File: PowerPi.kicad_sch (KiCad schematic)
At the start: 34 parts, among them J1 2444, J3 Conn_01x02, J6 Raspberry_Pi_2_3, J8 2444, Q1 30V 4A 44mΩ, Q2 50nA 150V 200mW 200mA, Q3 30V 4A 44mΩ, U1 XL4015

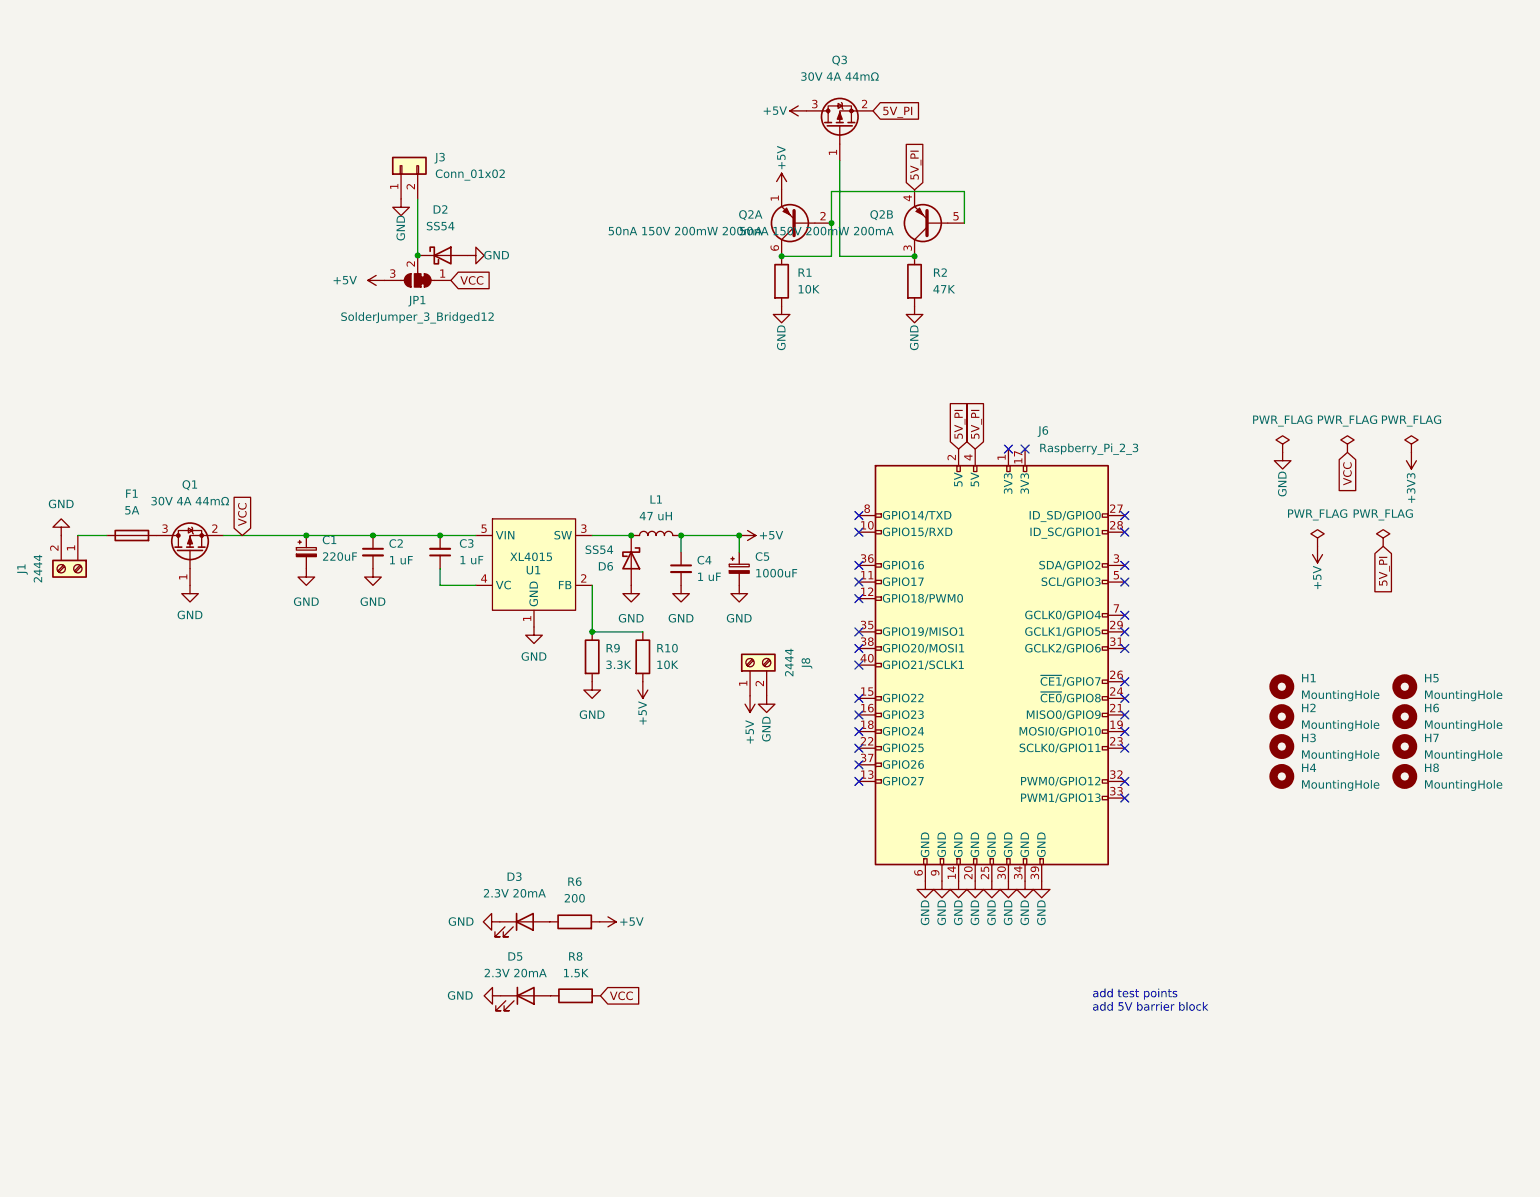
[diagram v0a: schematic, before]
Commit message: Production Changes
Added LDO Naming to R.silk
Fan JST XH pin +5 and GND swapped to match standard fans
5V pwr LED resistor was 200R now 1KR
24v pwr LED was 1.5k now 10k
Changed sch symbol for XH to not have screws
Added boxes to schematic layout
Added title box entries to schematic
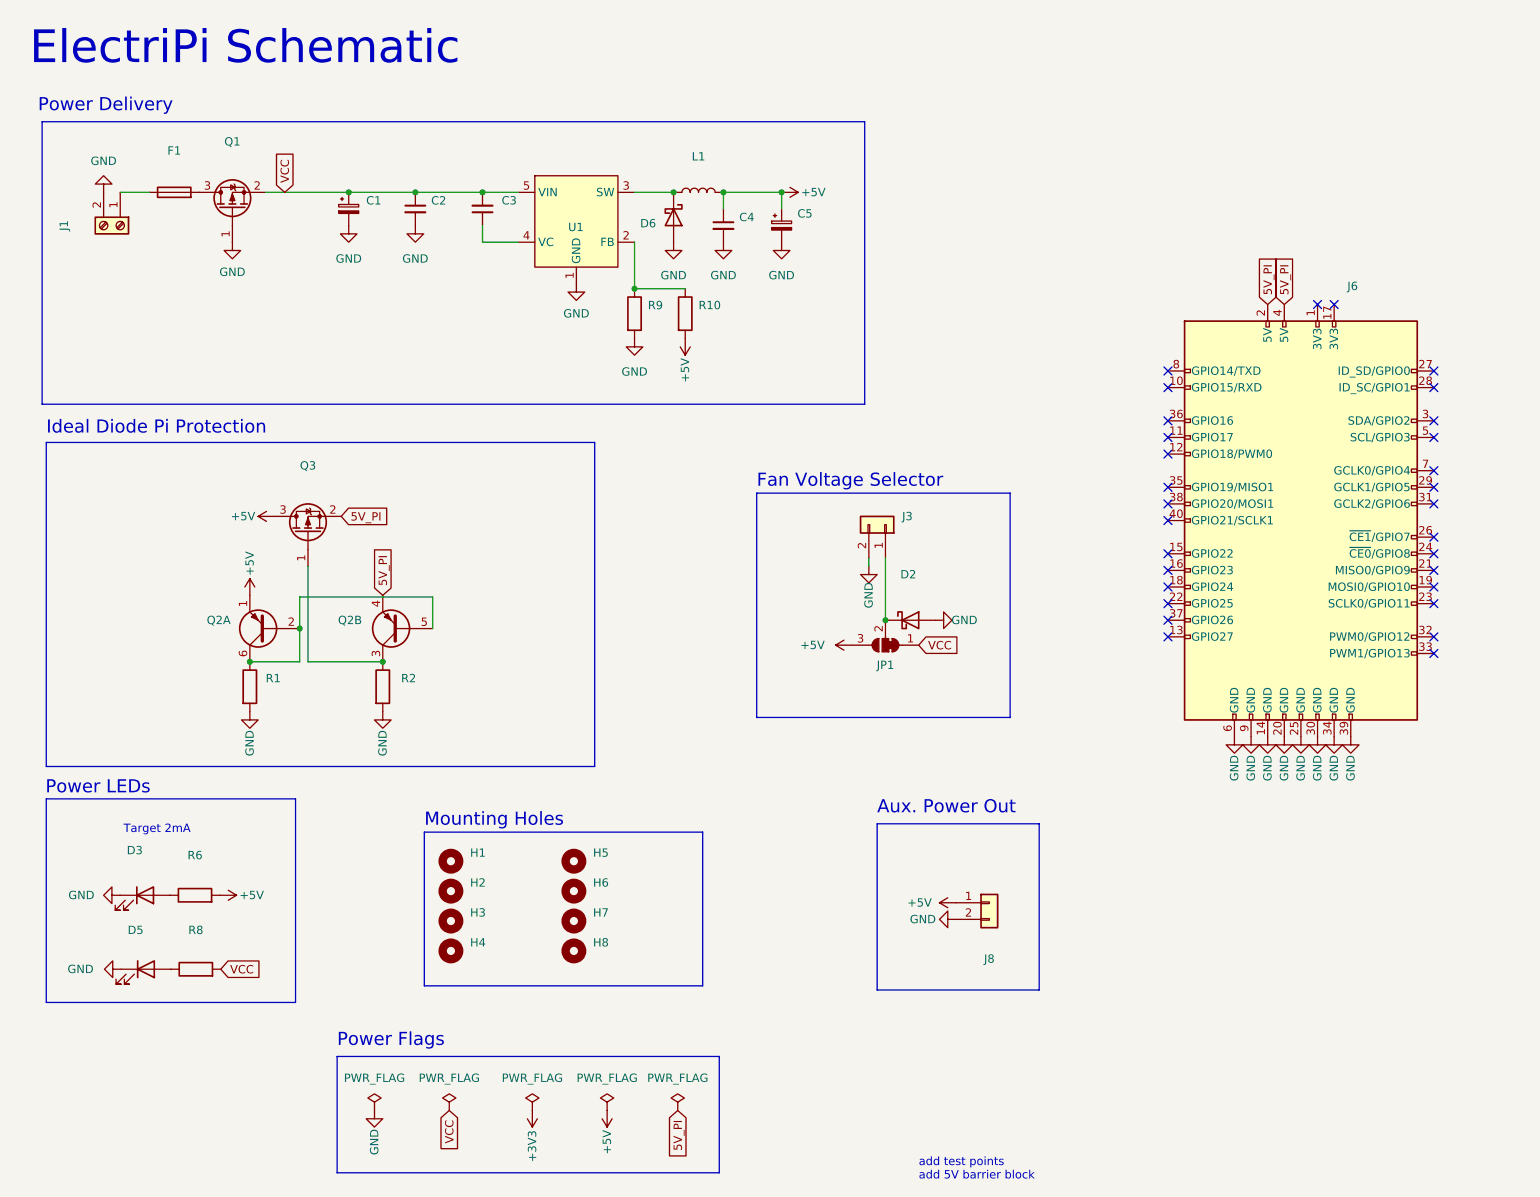
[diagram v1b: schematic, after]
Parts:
- C1: value 220uF -> (none); footprint Capacitor_SMD:CP_Elec_10x10 -> (none)
- C2, C3, C4: value 1 uF -> (none); footprint Capacitor_SMD:C_0603_1608Metric -> (none)
- C5: value 1000uF -> (none); footprint Capacitor_SMD:CP_Elec_8x10 -> (none)
- D2, D6: value SS54 -> (none); footprint Diode_SMD:D_SMA -> (none)
- D3, D5: value 2.3V 20mA -> (none); footprint LED_SMD:LED_0603_1608Metric -> (none)
- F1: value 5A -> (none); footprint Fuse:Fuseholder_Blade_Mini_Keystone_3568 -> (none); ManfNum 0154005.DR -> Keystone 3568; abv.Footprint SMD-2_5.03x9.73x3.81 -> (none)
- H1, H2, H3, H4: value MountingHole -> (none); footprint MountingHole:MountingHole_2.7mm_M2.5_DIN965_Pad -> (none)
- H5, H6, H7, H8: value MountingHole -> (none); footprint MountingHole:MountingHole_3.5mm -> (none)
- J1: value 2444 -> (none); footprint TerminalBlock_4Ucon:TerminalBlock_4Ucon_1x02_P3.50mm_Horizontal -> (none)
- J3: value Conn_01x02 -> (none); footprint Connector_JST:JST_XH_B2B-XH-A_1x02_P2.50mm_Vertical -> (none)
- J6: value Raspberry_Pi_2_3 -> (none); footprint Connector_PinSocket_2.54mm:PinSocket_2x20_P2.54mm_Vertical -> (none)
- J8: value 2444 -> (none); footprint Connector_JST:JST_XH_B2B-XH-A_1x02_P2.50mm_Vertical -> (none); symbol Connector:Screw_Terminal_01x02 -> Connector_Generic:Conn_01x02; now in the parts list
- JP1: value SolderJumper_3_Bridged12 -> (none); footprint Jumper:SolderJumper-3_P1.3mm_Bridged2Bar12_RoundedPad1.0x1.5mm -> (none)
- L1: value 47 uH -> (none); footprint Inductor_SMD:L_12x12mm_H6mm -> (none)
- Q1, Q3: value 30V 4A 44mΩ -> (none); footprint Package_TO_SOT_SMD:SOT-23 -> (none)
- Q2: value 50nA 150V 200mW 200mA -> (none); footprint Package_TO_SOT_SMD:SOT-363_SC-70-6 -> (none)
- R1: value 10K -> (none); footprint Resistor_SMD:R_0402_1005Metric -> (none)
- R10: value 10K -> (none); footprint Resistor_SMD:R_0603_1608Metric -> (none)
- R2: value 47K -> (none); footprint Resistor_SMD:R_0402_1005Metric -> (none)
- R6: value 200 -> (none); footprint Resistor_SMD:R_0402_1005Metric -> (none)
- R8: value 1.5K -> (none); footprint Resistor_SMD:R_0402_1005Metric -> (none)
- R9: value 3.3K -> (none); footprint Resistor_SMD:R_0603_1608Metric -> (none)
- U1: value XL4015 -> (none); footprint Package_TO_SOT_SMD:TO-263-5_TabPin3 -> (none)
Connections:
- net GND: now also J3.2 (Pin_2); no longer J3.1 (Pin_1)
- net at D2.1 (K), JP1.2 (C): now also J3.1 (Pin_1); no longer J3.2 (Pin_2)
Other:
- note added: "Aux. Power Out"
- note added: "ElectriPi Schematic"
- note added: "Fan Voltage Selector"
- note added: "Ideal Diode Pi Protection"
- note added: "Mounting Holes"
- note added: "Power Delivery"
- note added: "Power Flags"
- note added: "Power LEDs"
- note added: "Target 2mA"
- title: (none) -> ElectriPi
- moved on the sheet: C1, C2, C3, C4, C5, D2, D3, D5, D6, F1, H1, H2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
